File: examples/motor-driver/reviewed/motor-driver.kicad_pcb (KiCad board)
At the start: 2 copper layers, 88 x 50 mm, 19 parts, among them J1 VM 2.7-10.8V, J2 MOTOR A, J3 MOTOR B, J4 LOGIC, U1 DRV8833PW

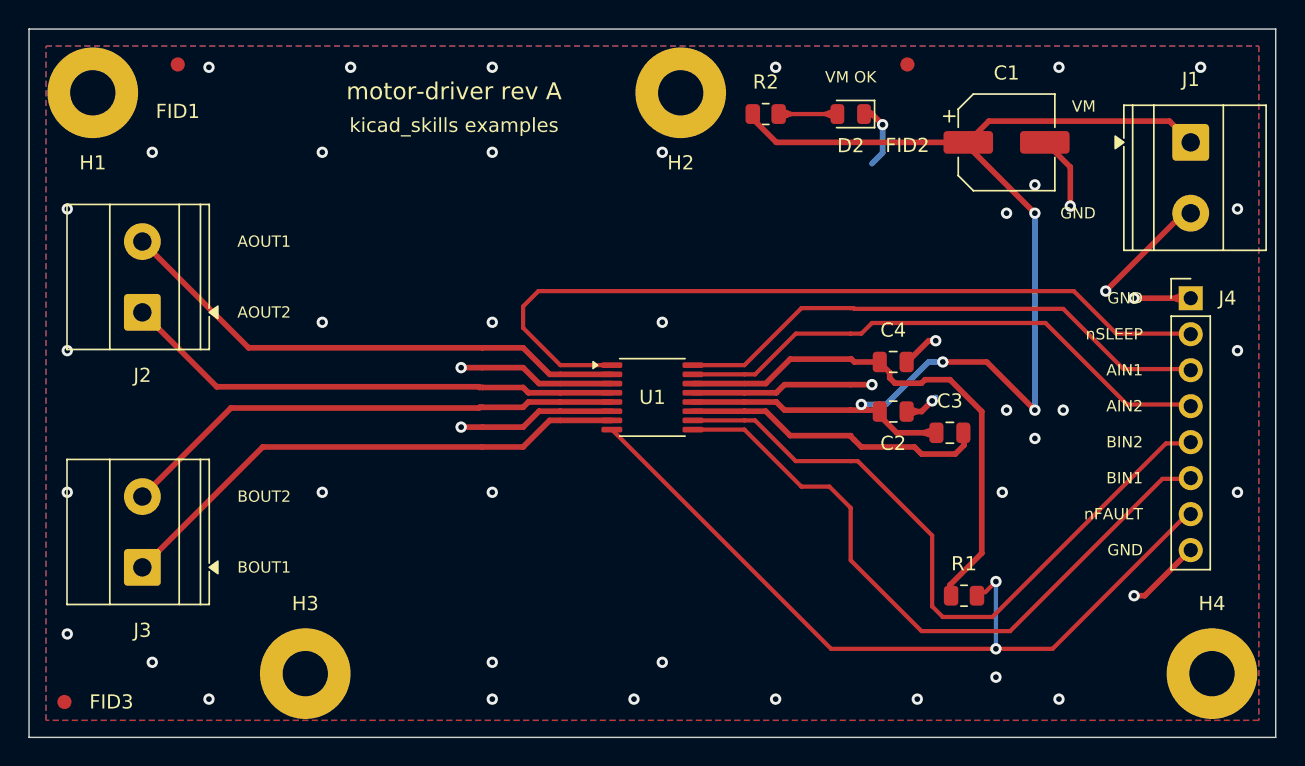
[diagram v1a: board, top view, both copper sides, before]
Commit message: Regenerate the five boards with the sliding, corner-anchored rim ring
Rim gaps against `emc.stitching_pitch`'s 18 mm, per reviewed board, before
and after: buck-5v 3 at 26.0 mm to 1 at 19.3, fpga-audio 3 at 20.0 to 3 at
19.7, motor-driver 7 at 32.6 to 2 at 24.0, opamp-filter 5 at 28.0 to 1 at
19.0, pico-carrier 6 at 40.0 to none at all. Twenty-four gaps become seven,
and the widest on any board falls from 40 mm to 24.

All five reviewed boards are DRC-clean and pass their own gate policy; the
as-generated variants keep the violations that are their whole point.

What is left is mostly 19 mm against a limit of 18 - stations whose slide ran
out before the arc did - which is a gap-filling pass rather than a wider
slide, since a via that walks further than half a step is standing at its
neighbour's station.

Co-Authored-By: Claude Fable 5 <noreply@anthropic.com>
Claude-Session: https://claude.ai/code/session_01DUj7Ltu92tWg159mCSacwY
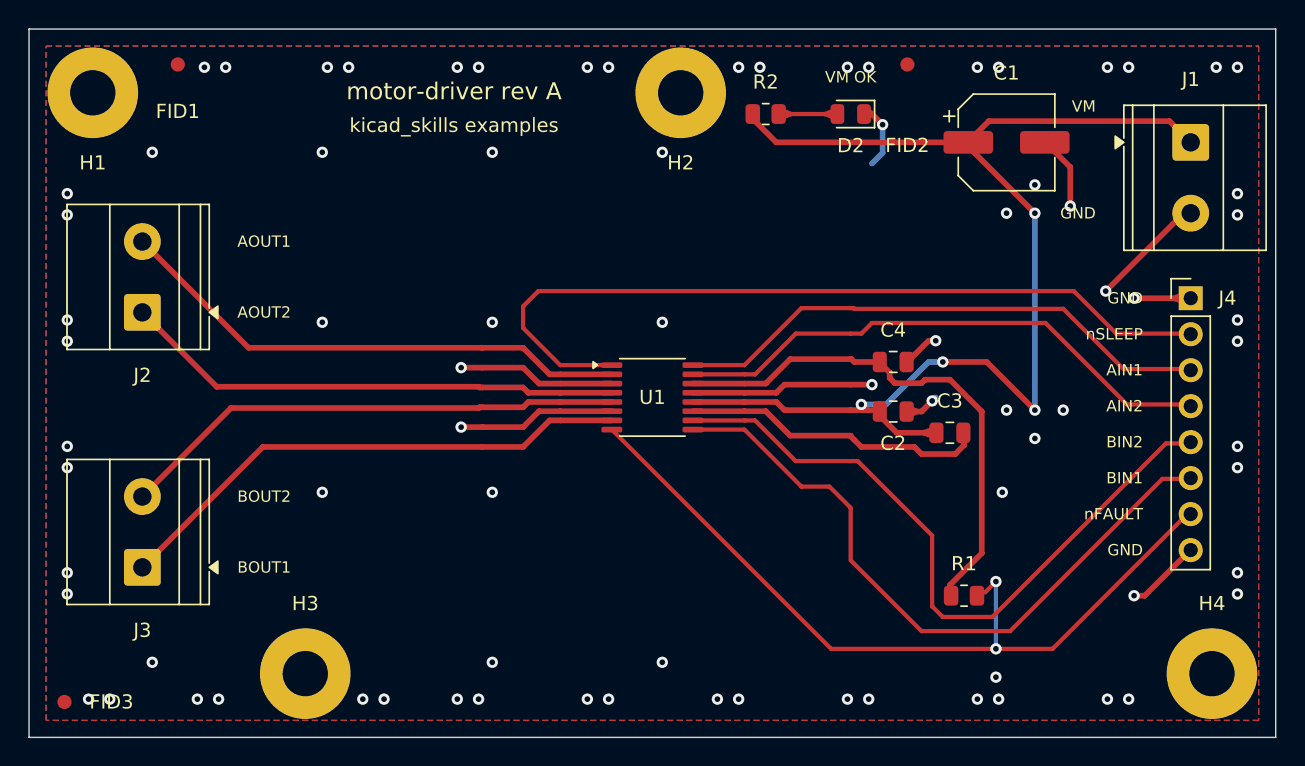
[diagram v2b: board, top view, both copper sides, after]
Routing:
- net GND: vias 48 -> 81

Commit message: Regenerate the five boards: no rim stitching gap left on any of them
`emc.stitching_pitch` reported 24 gaps across the five reviewed boards, the
widest 40 mm against a limit of 18. It now reports nothing on any of them.
Vias on the reviewed boards: buck 119 to 124, fpga 235 to 244, motor 87 to
94, opamp 69 to 70, carrier 89 to 90 - thirty-three vias for the whole set,
which is what a rim ring costs when it is allowed to place them where the
board has room rather than only where the grid fell.

All five are DRC-clean and pass their own gate policy.

Co-Authored-By: Claude Fable 5 <noreply@anthropic.com>
Claude-Session: https://claude.ai/code/session_01DUj7Ltu92tWg159mCSacwY
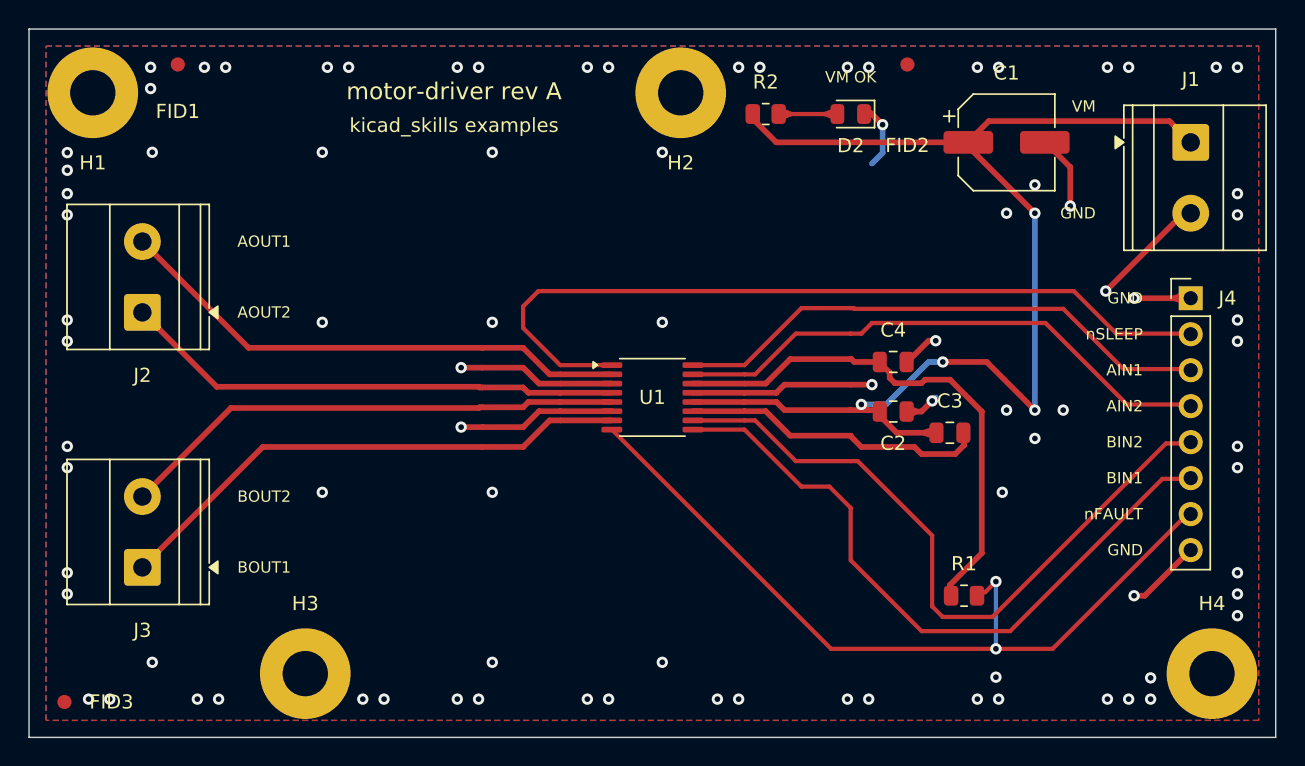
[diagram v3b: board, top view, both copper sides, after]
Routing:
- net GND: vias 81 -> 88
